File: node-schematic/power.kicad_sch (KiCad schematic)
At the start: 14 parts, among them J4 B2B-PH-K-S, U4 MAX17048G_T10

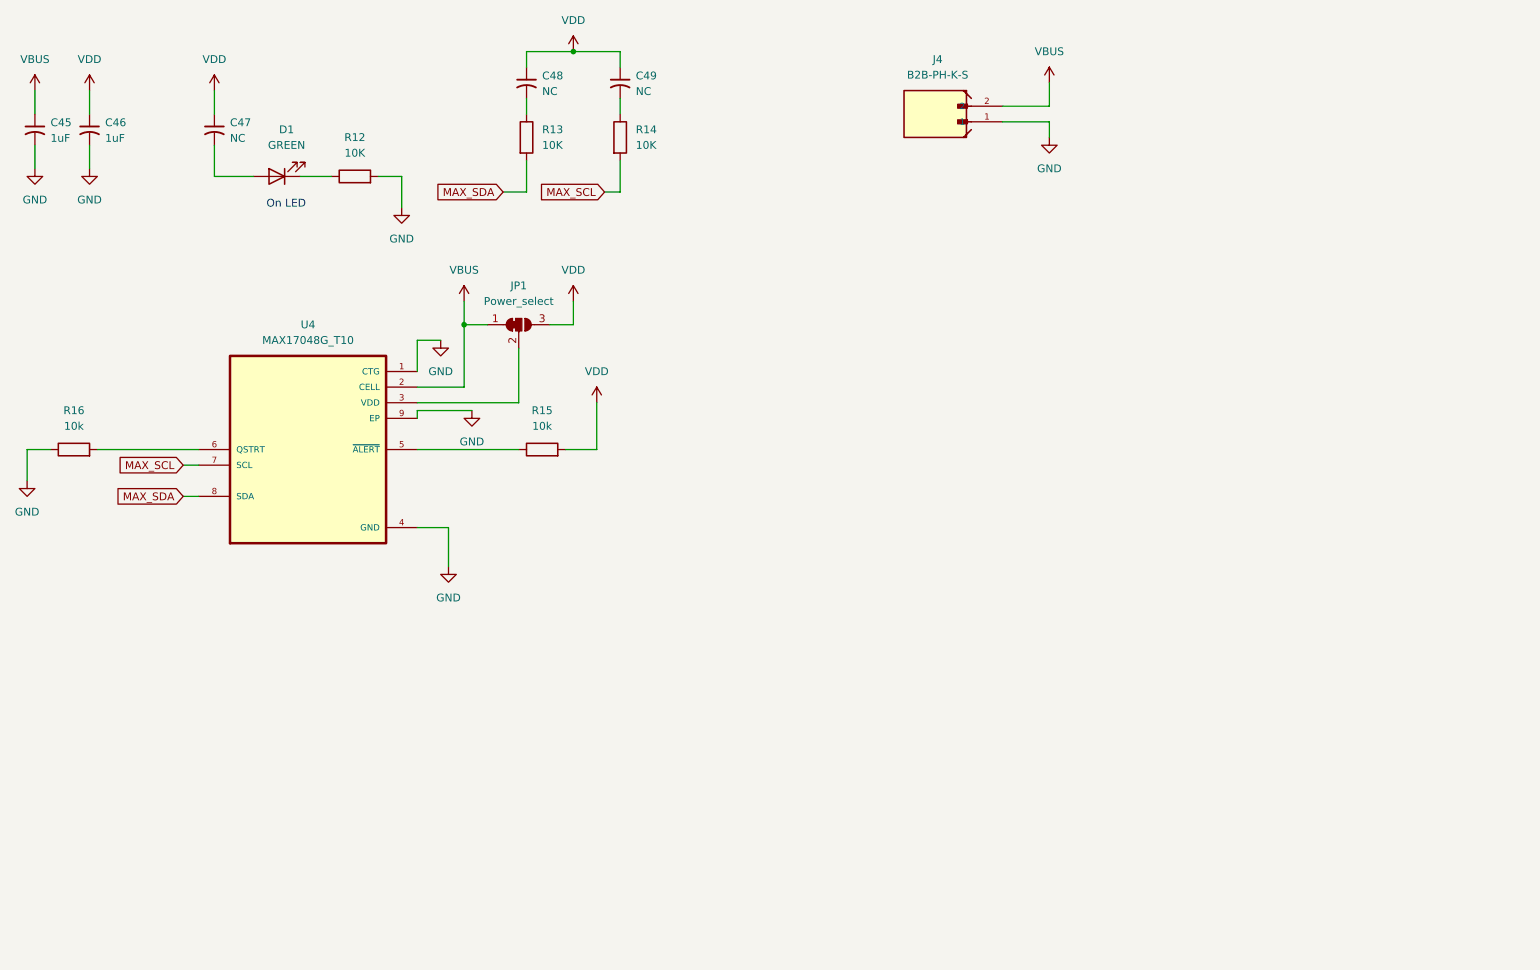
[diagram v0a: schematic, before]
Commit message: completed pcb and box
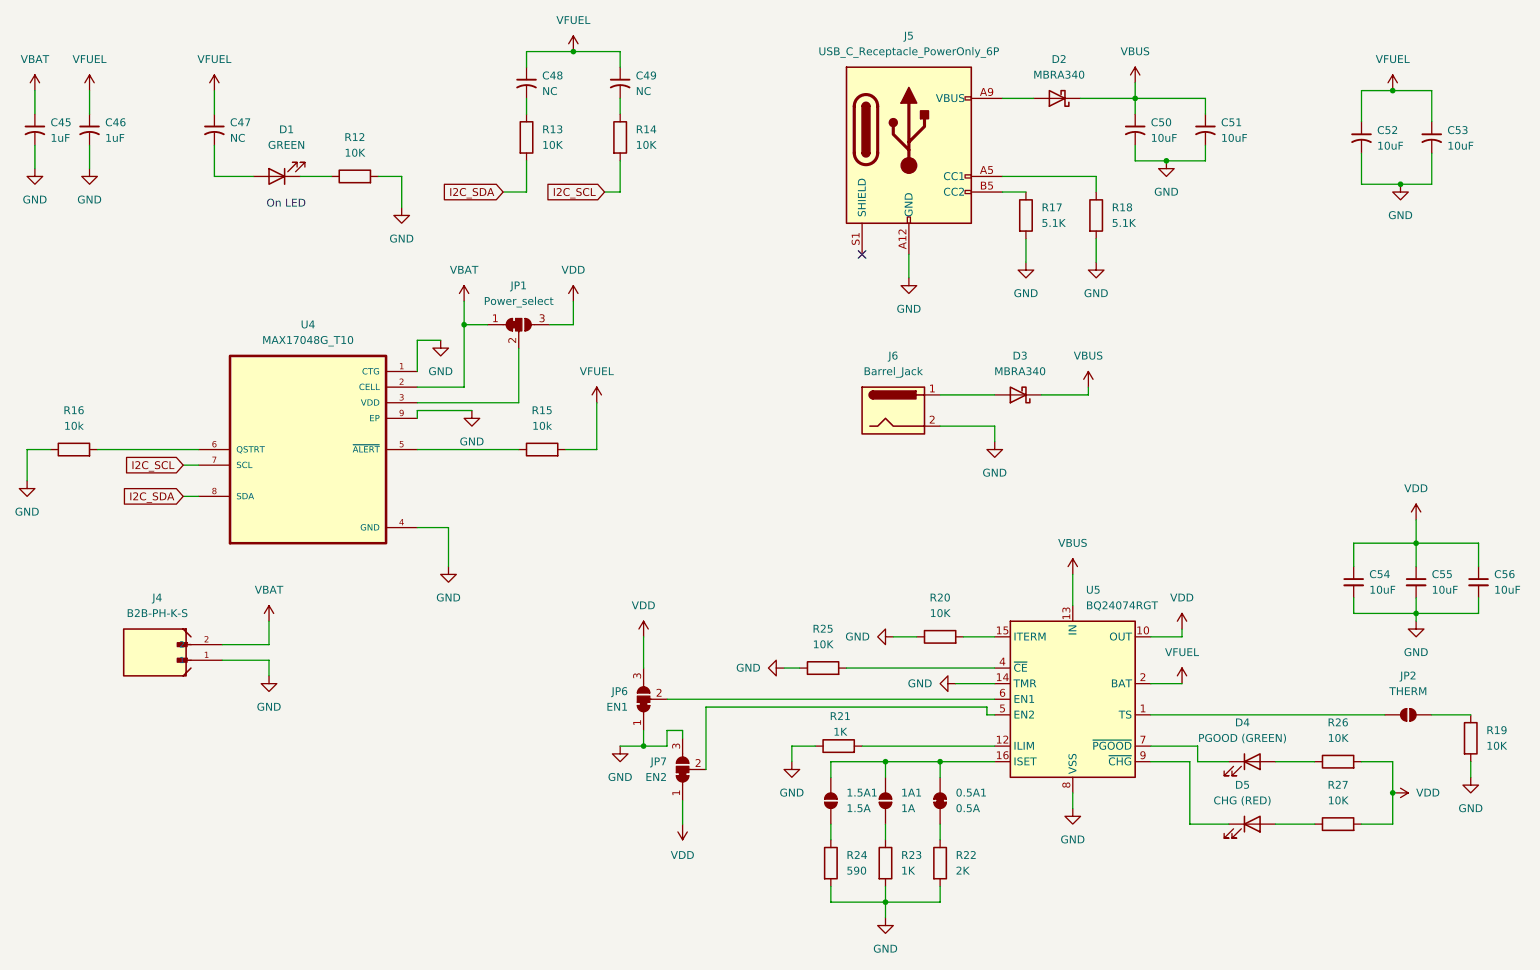
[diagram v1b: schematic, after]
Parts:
- added 0.5A1: 0.5A, Jumper:SolderJumper-2_P1.3mm_Bridged_RoundedPad1.0x1.5mm, symbol Jumper:SolderJumper_2_Bridged
- added 1.5A1: 1.5A, Jumper:SolderJumper-2_P1.3mm_Open_RoundedPad1.0x1.5mm, symbol Jumper:SolderJumper_2_Open
- added 1A1: 1A, Jumper:SolderJumper-2_P1.3mm_Open_RoundedPad1.0x1.5mm, symbol Jumper:SolderJumper_2_Open
- added C50, C51, C52, C53: 10uF, Capacitor_SMD:C_0201_0603Metric, symbol Device:C_Small_US
- added C54, C55, C56: 10uF, Capacitor_SMD:C_0201_0603Metric, symbol Device:C_Small
- added D2, D3: MBRA340, Diode_SMD:D_SMA, symbol Diode:MBRA340
- added D4: PGOOD (GREEN), LED_SMD:LED_0201_0603Metric, symbol Device:LED
- added D5: CHG (RED), LED_SMD:LED_0201_0603Metric, symbol Device:LED
- added J5: USB_C_Receptacle_PowerOnly_6P, Connector_USB:USB_C_Receptacle_GCT_USB4125-xx-x_6P_TopMnt_Horizontal, symbol Connector:USB_C_Receptacle_PowerOnly_6P
- added J6: Barrel_Jack, Connector_BarrelJack:BarrelJack_CUI_PJ-036AH-SMT_Horizontal, symbol Connector:Barrel_Jack
- added JP2: THERM, Jumper:SolderJumper-2_P1.3mm_Open_RoundedPad1.0x1.5mm, symbol Jumper:SolderJumper_2_Open
- added JP6: EN1, Jumper:SolderJumper-3_P1.3mm_Bridged12_RoundedPad1.0x1.5mm_NumberLabels, symbol Jumper:SolderJumper_3_Bridged12
- added JP7: EN2, Jumper:SolderJumper-3_P1.3mm_Bridged12_RoundedPad1.0x1.5mm_NumberLabels, symbol Jumper:SolderJumper_3_Bridged12
- added R17, R18: 5.1K, Resistor_SMD:R_0201_0603Metric, symbol Device:R
- added R19, R20, R25, R26, R27: 10K, Resistor_SMD:R_0201_0603Metric, symbol Device:R
- added R21, R23: 1K, Resistor_SMD:R_0201_0603Metric, symbol Device:R
- added R22: 2K, Resistor_SMD:R_0201_0603Metric, symbol Device:R
- added R24: 590, Resistor_SMD:R_0201_0603Metric, symbol Device:R
- added U5: BQ24074RGT, Package_DFN_QFN:VQFN-16-1EP_3x3mm_P0.5mm_EP1.6x1.6mm, symbol Battery_Management:BQ24074RGT
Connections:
- net GND: now also C50.2, C51.2, C52.2, C53.2, C54.2, C55.2, C56.2, J5.A12 (GND), J5.B12 (GND), J6.2, JP6.1 (A), JP7.3 (B), R17.2, R18.2, R19.2, R20.1, R21.1, R22.2, R23.2, R24.2, R25.1, U5.14 (TMR), U5.17 (VSS), U5.8 (VSS)
- net VBUS: now also C50.1, C51.1, D2.1 (K), D3.1 (K), U5.13 (IN); no longer C45.1, J4.2, JP1.1 (A), U4.2 (CELL)
- net VDD: now also C54.1, C55.1, C56.1, JP6.3 (B), JP7.1 (A), R26.2, R27.2, U5.10 (OUT), U5.11 (OUT); no longer C46.1, C47.1, C48.1, C49.1, R15.2
- net MAX_SCL renamed I2C_SCL
- net MAX_SDA renamed I2C_SDA
- new net: 1.5A1.1 (A), R24.1
- new net: 0.5A1.2 (B), 1.5A1.2 (B), 1A1.2 (B), U5.16 (ISET)
- new net: D5.1 (K), U5.9 (~{CHG})
- new net: D5.2 (A), R27.1
- new net: JP7.2 (C), U5.5 (EN2)
- new net: D4.1 (K), U5.7 (~{PGOOD})
- new net: D4.2 (A), R26.1
- new net: J5.A5 (CC1), R18.1
- new net: D2.2 (A), J5.A9 (VBUS), J5.B9 (VBUS)
- new net: J5.B5 (CC2), R17.1
- new net: JP2.1 (A), U5.1 (TS)
- new net: JP2.2 (B), R19.1
- new net: D3.2 (A), J6.1
- new net: 0.5A1.1 (A), R22.1
- new net: 1A1.1 (A), R23.1
- new net: JP6.2 (C), U5.6 (EN1)
- new net: R21.2, U5.12 (ILIM)
- new net: R20.2, U5.15 (ITERM)
- new net: R25.2, U5.4 (~{CE})
- new net VBAT: C45.1, J4.2, JP1.1 (A), U4.2 (CELL)
- new net VFUEL: C46.1, C47.1, C48.1, C49.1, C52.1, C53.1, R15.2, U5.2 (BAT), U5.3 (BAT)
- no-connect marks 0 -> 1
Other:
- moved on the sheet: J4
